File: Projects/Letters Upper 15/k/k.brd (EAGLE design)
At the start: 16.5 x 21.6 mm, 42 parts

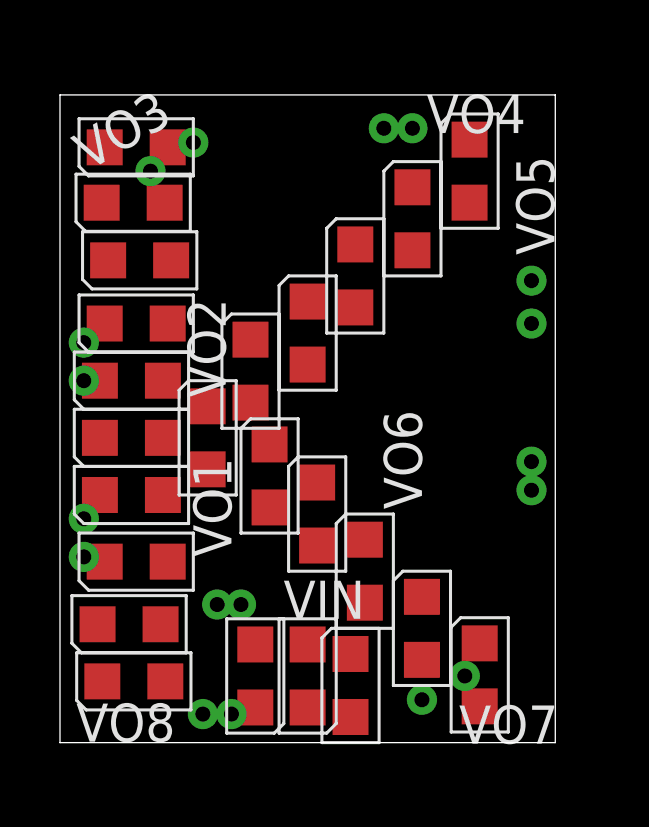
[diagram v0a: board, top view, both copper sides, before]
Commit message: 
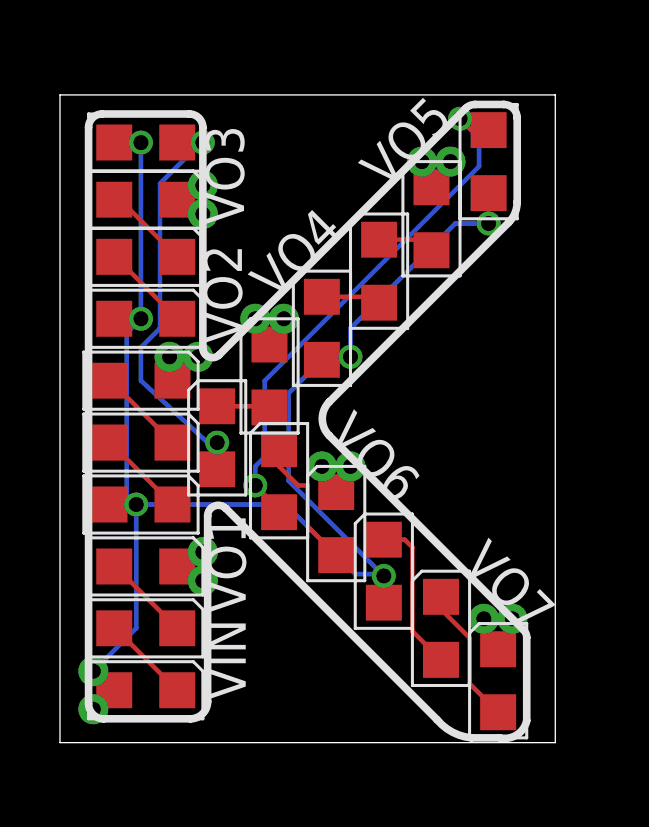
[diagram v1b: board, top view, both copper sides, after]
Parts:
- removed LED22, LED23, LED24: (no value), CyberRailGuru:LED_0805
- removed VO15, VO16: (no value), CyberRailGuru:P1-20
- moved VO13 8.45 mm to (8.73, 9.21)
- moved VO9 7.68 mm to (4.60, 12.9)
- moved VO4 7.66 mm to (7.46, 14.1)
- moved VO11 6.23 mm to (6.51, 14.1)
- moved VO6 6.08 mm to (9.68, 9.21)
- moved VIN1 6.03 mm to (1.11, 1.11)
- moved VO10 5.84 mm to (4.76, 17.6)
- moved VO14 5.47 mm to (14.1, 4.13)
- moved VO5 5.39 mm to (12.1, 19.4)
- moved VIN 4.69 mm to (1.11, 2.38)
- moved VO8 4.55 mm to (4.76, 5.40)
- moved VO1 4.12 mm to (4.76, 6.35)
- moved VO2 2.97 mm to (3.65, 12.9)
- moved VO12 2.48 mm to (13.0, 19.4)
- moved VO7 2.48 mm to (15.1, 4.13)
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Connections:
- removed net N$1: LED22.C, LED23.A
- removed net N$2: LED23.C, LED24.A
- removed net N$5: LED24.C, VO16.TP, VO8.TP
- net VIN: no longer LED22.A
- net VOUT1: now also VO8.TP; no longer VO9.TP
- net VOUT2: now also VO9.TP; no longer VO10.TP
- net VOUT3: now also VO10.TP; no longer VO11.TP
- net VOUT4: now also VO11.TP; no longer VO12.TP
- net VOUT5: now also VO12.TP; no longer VO13.TP
- net VOUT6: now also VO13.TP; no longer VO14.TP
- net VOUT7: now also VO14.TP; no longer VO15.TP
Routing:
- net VIN: track 0.00 -> 52.2 mm, vias 0 -> 6
- net N$24: track 0.00 -> 17.9 mm, vias 0 -> 2
- net N$16: track 0.00 -> 13.9 mm, vias 0 -> 2
- net N$28: track 0.00 -> 5.20 mm
- net N$27: track 0.00 -> 4.64 mm
- net N$23: track 0.00 -> 4.50 mm
- net N$3: track 0.00 -> 2.95 mm
- net N$8: track 0.00 -> 2.95 mm
- net N$4: track 0.00 -> 2.95 mm
- net N$7: track 0.00 -> 2.95 mm
- net N$12: track 0.00 -> 2.95 mm
- net N$11: track 0.00 -> 2.89 mm
- net VOUT7: track 0.00 -> 2.42 mm
- net VOUT6: track 0.00 -> 2.10 mm
- net VOUT5: track 0.00 -> 2.10 mm
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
